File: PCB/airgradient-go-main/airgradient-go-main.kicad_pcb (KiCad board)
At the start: 4 copper layers, 62.9 x 88.3 mm, 194 parts, among them CN1 HCZZ0032-5, CN2 HCZZ0032-5, CN3 HCZZ0032-5, Q1 SIA445EDJ-T1-GE3, Q2 ZVN4106FTA_C508255, Q3 CSD83325L, Q4 SS8050-G, Q5 SI1308EDL, SW1 TS-1091C-A1B3-D2, SW2 TS-1091C-A1B3-D2, U1 W25N512GVEIG, U10 SGP41-D-R4, U11 PS1-CO-SMOKE-10k, U12 SHT4x, U13 SPL07-003, U14 LIS2DH12TR, U15 TMUX121NKGR_C22428404, U16 S12, U17 TCA6408ARGT, U18 TAU1113, U19 LM66200DRLR, U2 ZDSD512MLGEAG, U20 LP5036, U3 BQ27742YZFR-G1, U4 ESP32-C5-MINI-1, U5 BQ25628RYKR, U6 HYG-8503A, U7 TPL5010DDCR, U8 TPS63802DLAR, U9 TPS7A0228DQNR

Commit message: wip: checkpoint before Mac migration
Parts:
- U16: footprint S12-oaf:S12 -> S12-oaf:S12_rev2
- moved U16 11.9 mm to (155.1, 114.4)
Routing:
- net /SCL: track 354.0 -> 353.3 mm
- net GND: vias 147 -> 146

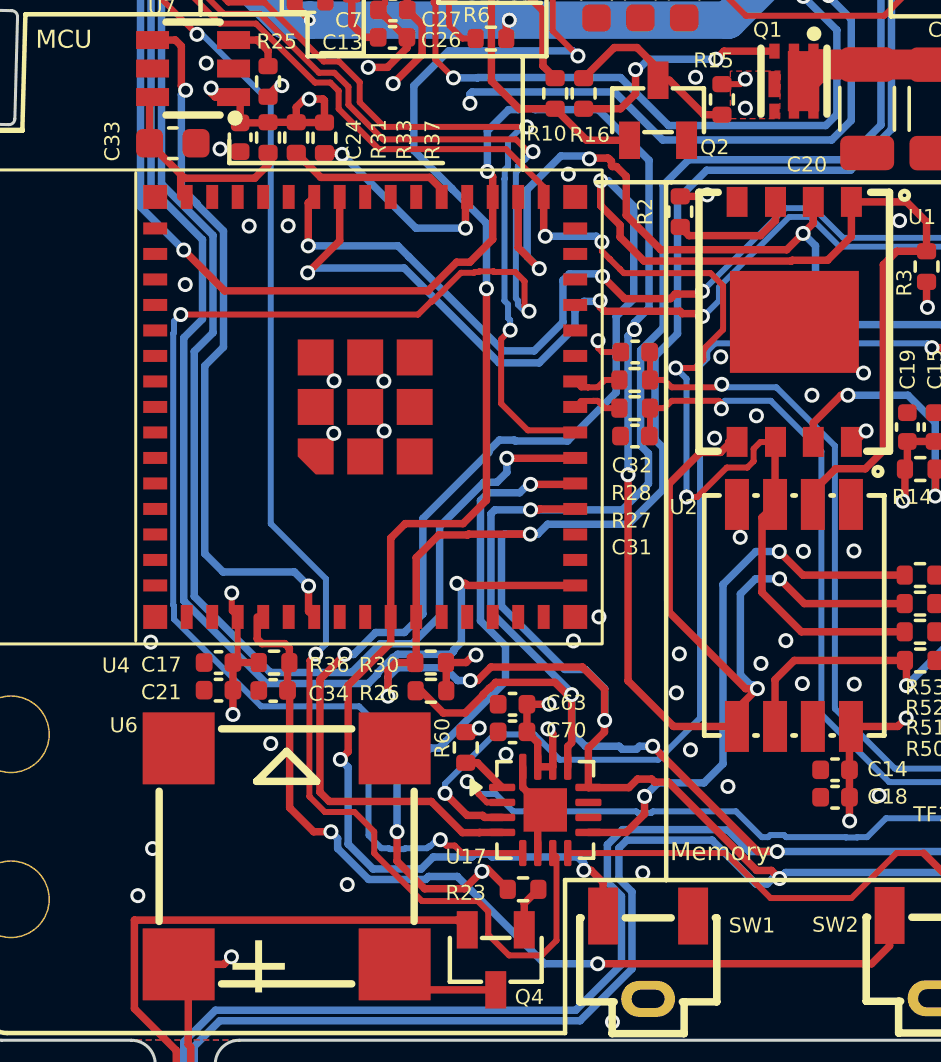
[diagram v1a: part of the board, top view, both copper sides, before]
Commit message: Lay out the RTC crystal; move ePaper CS to IO4
Schematic: ePaper CS moves from expander P7 to U4 IO4 (pad 8); P7 gets
an NC flag. The P7 route needed 5 vias through EN_PM1/BUZZ/PRTRG.

PCB (pcb-design skill, groups in design/.../layout/route.json):
- Y1/C77/C76 in the column between U4 and U2, next to U4 pads 16/17.
  XTAL_32K_P/N on F.Cu, 0 vias, 4.9/4.5 mm; C77 GND via 0.5/0.3.
- MOSI rerouted out of that column: U4 trunk -> U1.5 above the
  crystal (1 via), U1.5 -> U2.5 on its right side (2 vias).
- ePaper CS from IO4 under the module body to the old trunk (1 via);
  the old IO0 stub and the dead trunk ends are removed.
- Memory silk line split around the crystal; 8 references re-placed.

Checks: DRC 230 = baseline (0 new), 0 unconnected, parity 0. No new
bends, junctions, dangling ends or vias vs HEAD; unrelated nets
identical to HEAD. Accepted: I2C on B.Cu under Y1/C77 (RF-22, GND
plane between), CS at 0.2 mm.
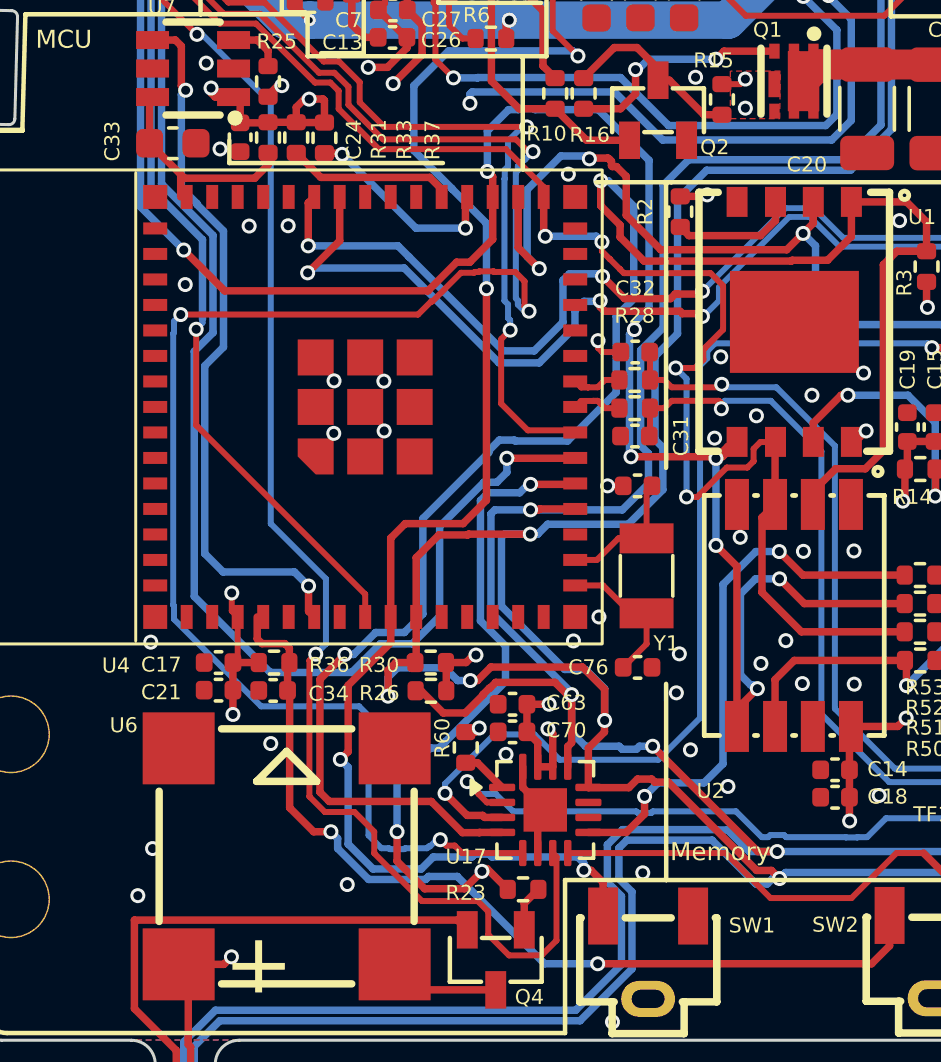
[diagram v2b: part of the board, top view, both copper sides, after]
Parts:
- added C76: 8.2pF/50V, Capacitor_SMD:C_0402_1005Metric, F.Cu at (123.6, 124.7)
- added C77: 8.2pF/50V, Capacitor_SMD:C_0402_1005Metric, F.Cu at (123.6, 118.6)
- added Y1: 32.768kHz CL6pF, Crystal:Crystal_SMD_3215-2Pin_3.2x1.5mm, F.Cu at (123.9, 121.6)
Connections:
- U4 pad 16: /ePaper CS -> /XTAL_32K_P
- U4 pad 17: /IO1 -> /XTAL_32K_N
- U4 pad 8: /IO4 -> /ePaper CS
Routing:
- net /ePaper CS: track 109.4 -> 95.2 mm
- net /MOSI: track 143.2 -> 134.2 mm, vias 8 -> 10
- net /XTAL_32K_P: track 0.00 -> 4.89 mm
- net /XTAL_32K_N: track 0.00 -> 4.50 mm
- net GND: track 54.5 -> 55.0 mm, vias 146 -> 147

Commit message: Move I2C to the C5 LP I2C pins; WD_RST to IO4, ePaper CS to IO6
The ESP32-C5 LP I2C is fixed to GPIO2 (SDA) and GPIO3 (SCL) by the LP IO
MUX, and v2.1 had the bus on IO6/IO7 (IO7 is not an LP pin). Moving it
lets the LP core read the sensors in offline mode while the HP core
stays in deep sleep (Sam's proposal, R-LP-01..03).

- U4 IO2 = SDA, IO3 = SCL, IO4 = WD_RST (TPL5010 DONE stays on an LP
  pin so the LP core can feed it), IO6 = ePaper CS, IO7 unused.
- WD_RST takes IO4 rather than IO6: from pad 10 the route to U7 needed
  5 vias; from pad 8 it reuses the old CS path with one via.
- Layout: SDA/SCL 2 vias each, WD_RST 1, CS 1, two old vias removed.
  DRC 230 = baseline, 0 unconnected, parity 0; no footprint moved.

Firmware: PIN_I2C_SDA = GPIO2, PIN_I2C_SCL = GPIO3, PIN_EXT_WDT = GPIO4,
PIN_DISPLAY_CS = GPIO6; guard PIN_ACCEL_INT (GPIO3) to V1.
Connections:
- U4 pad 10: /SCL -> /ePaper CS
- U4 pad 19: /SDA -> /IO7
- U4 pad 6: /WD_RST -> /SDA
- U4 pad 7: /IO3 -> /SCL
- U4 pad 8: /ePaper CS -> /WD_RST
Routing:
- net /ePaper CS: track 95.2 -> 103.7 mm
- net /SDA: track 341.5 -> 349.0 mm, vias 17 -> 19
- net /WD_RST: track 23.9 -> 23.2 mm
- net /SCL: track 353.3 -> 353.4 mm, vias 18 -> 20

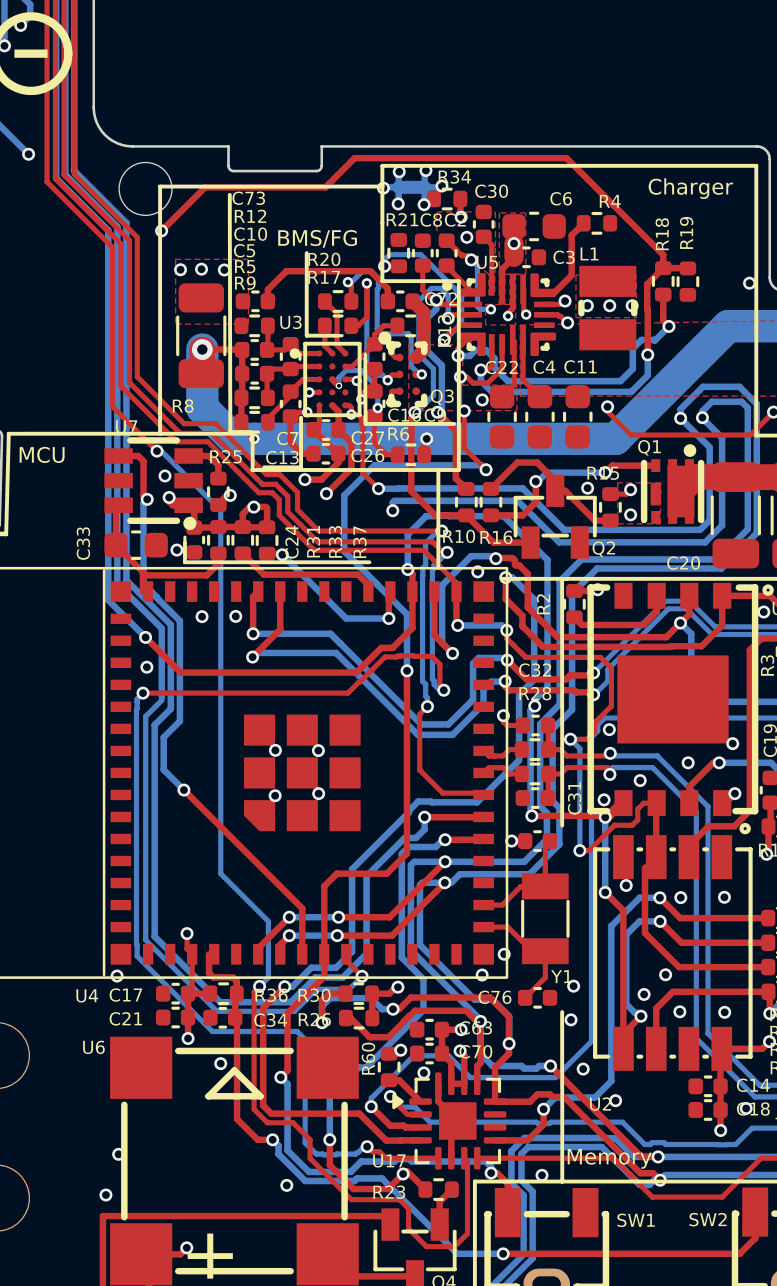
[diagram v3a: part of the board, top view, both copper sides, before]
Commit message: Route I2C_INT from U5 and U17 to IO7
Expander branch (group exp-int): U17 pin 11 -> U4 pad 19, 15.6 mm,
4 vias; PRTRG dips 0.24 mm under the first via (group prtrg-dip).

Charger branch: U5 pin 11 was walled in, so
- the SDA escape via moves 0.2 mm up under the SCL via, with its F.Cu
  stub and In2 jog redrawn (group u5-i2c-escape);
- pin 11 leaves at 0.15 mm between pad 10 and the SDA via to a via
  0.25 mm from L1's SYS pad (group int-u5-escape);
- the trace runs 51 mm on B.Cu round the west end of the charger's
  power band, under the module body 3 mm clear of the antenna
  keepout, and joins the expander branch (group int-chg-west). No
  way south exists between x 16 and 34 on F.Cu, In2 or B.Cu.

I2C_INT: 68 mm, 7 vias 0.5/0.3. Zones refilled. DRC 230 = baseline,
0 unconnected, parity 0; pcb_check has no new FAIL (min width 0.15 =
DFM floor, one more RT-05 detour). TP1-TP17 that pcb_import re-adds
were deleted again; no footprint moved.
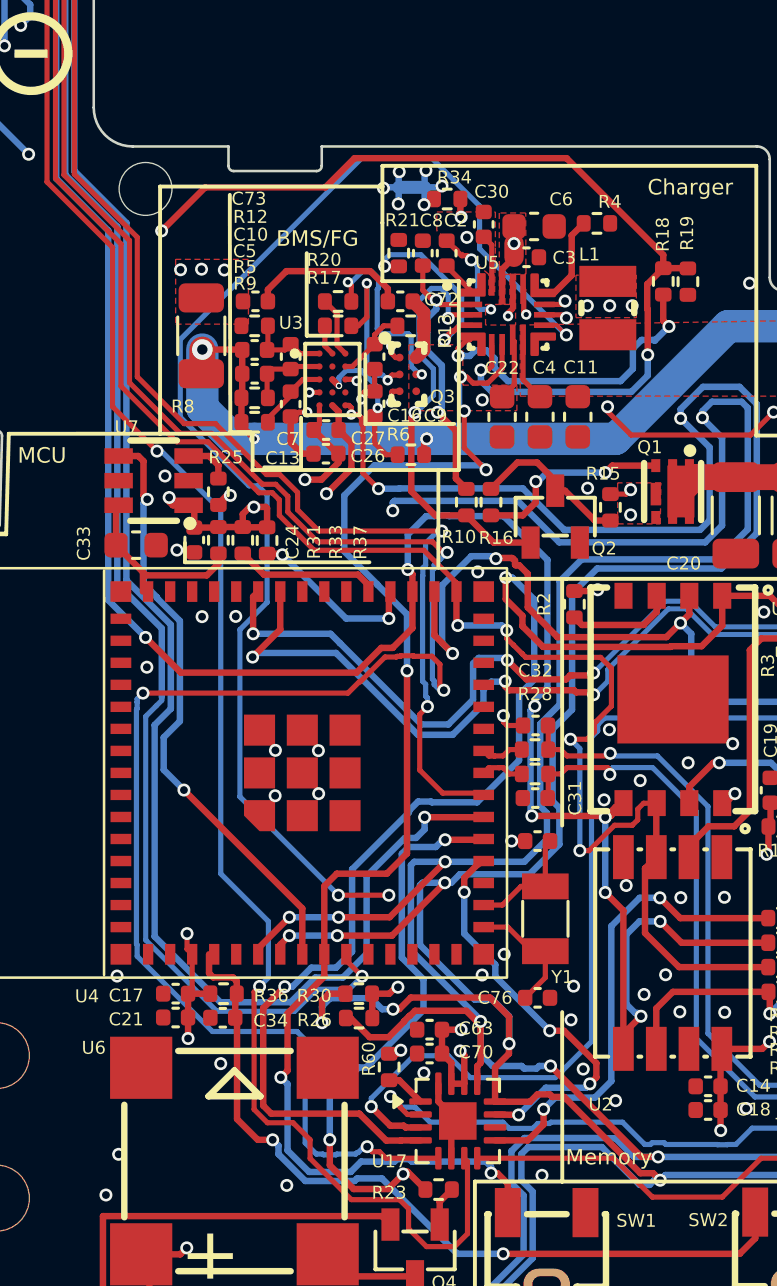
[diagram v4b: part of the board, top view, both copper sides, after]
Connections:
- U17 pad 11: unconnected-(U17-~{INT}-Pad11) -> /I2C_INT
- U4 pad 19: /IO7 -> /I2C_INT
- U5 pad 11: unconnected-(U5-~{INT}-Pad11) -> /I2C_INT
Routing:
- net /I2C_INT: track 0.00 -> 68.0 mm, vias 0 -> 7
